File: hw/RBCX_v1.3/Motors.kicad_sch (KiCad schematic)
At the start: 83 parts

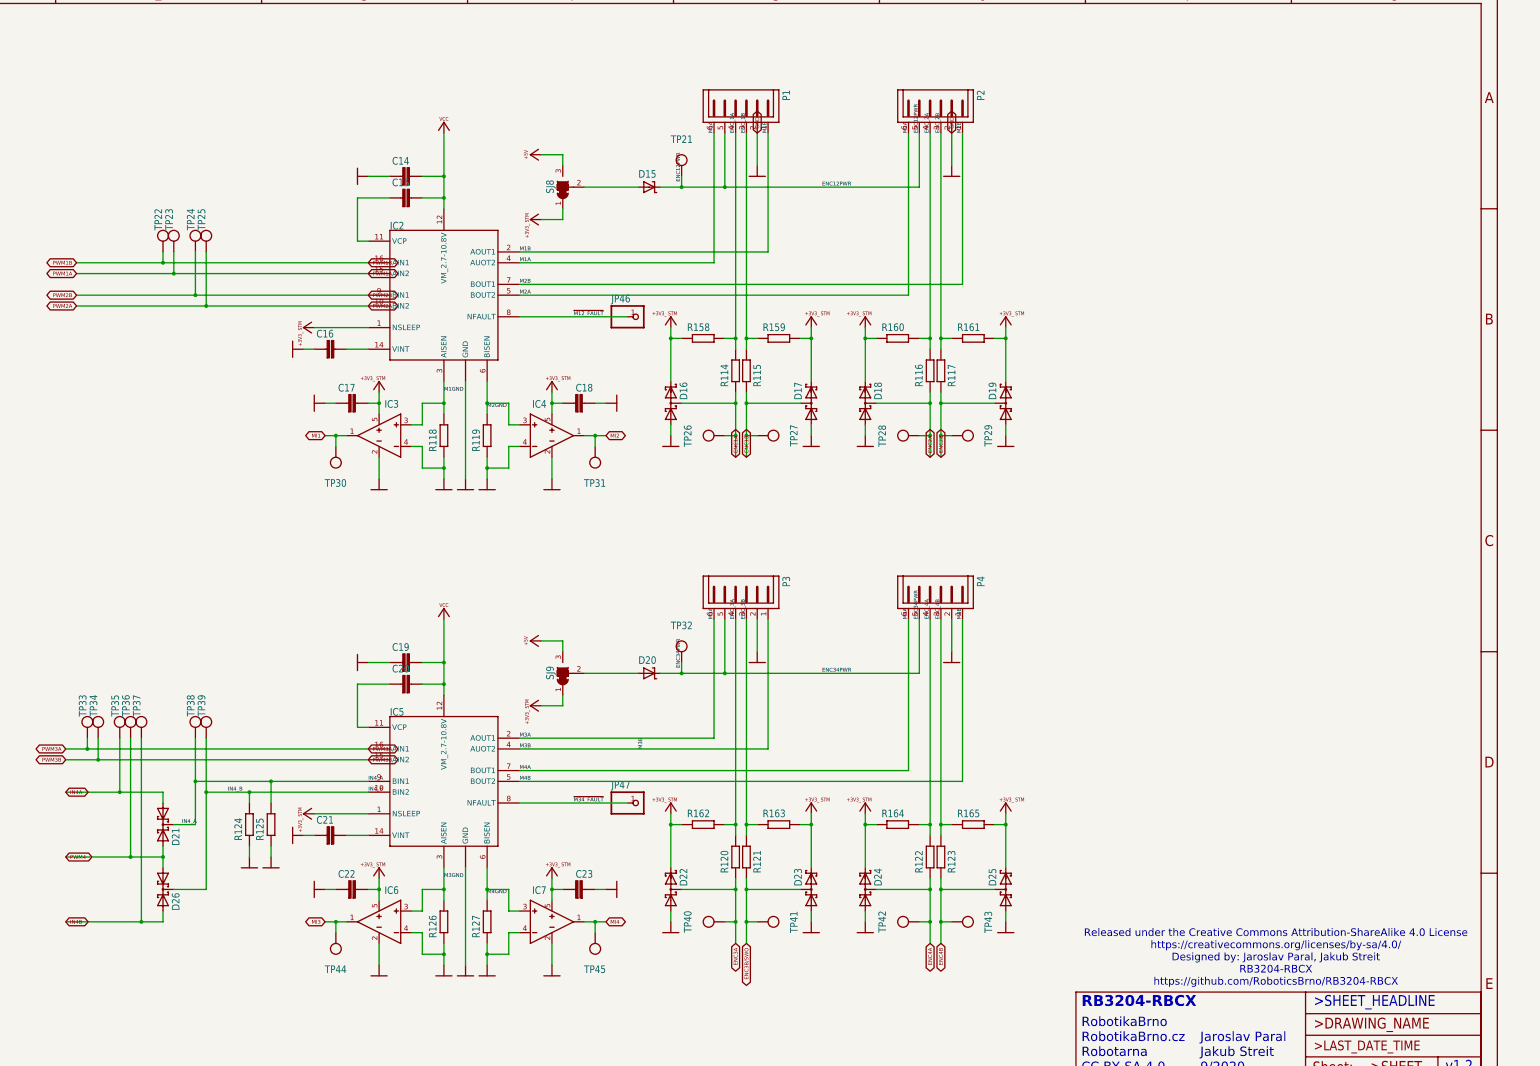
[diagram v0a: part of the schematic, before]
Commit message: Remove stepdowns, Micro-USB; fixup region names
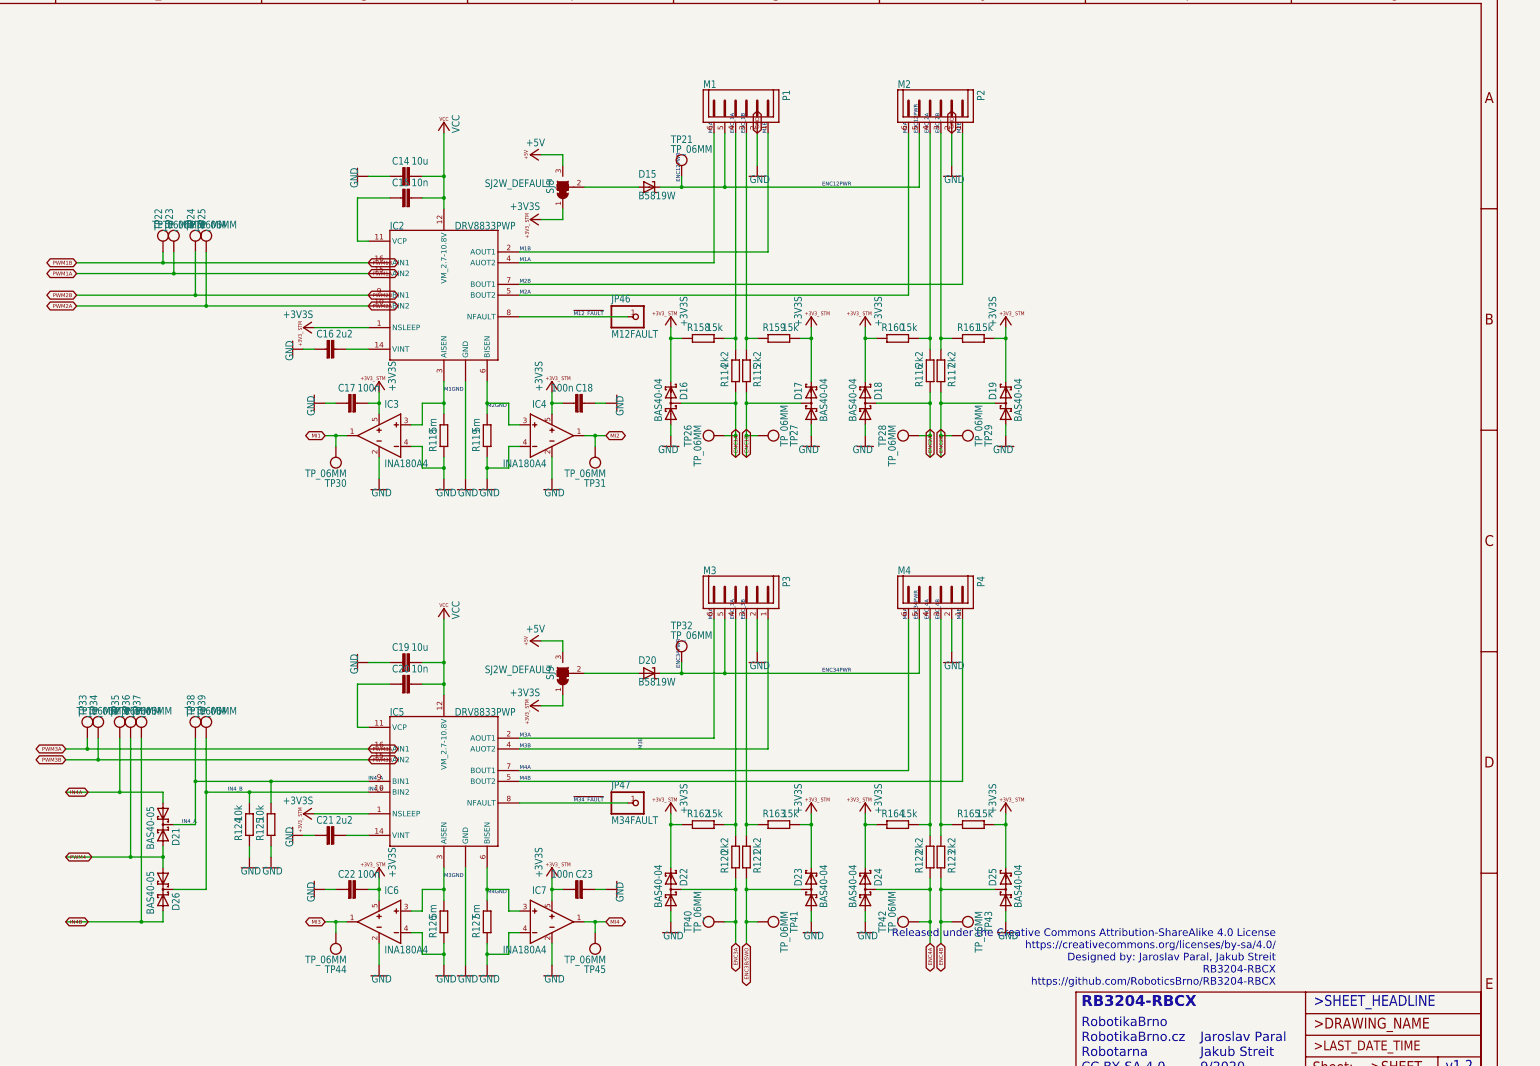
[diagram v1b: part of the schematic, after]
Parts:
- C14, C19: footprint (none) -> RBCX:C0805
- C15, C17, C18, C20, C22, C23: footprint (none) -> RBCX:C0402
- C16, C21: footprint (none) -> RBCX:C0603
- D15, D20: footprint (none) -> RBCX:SOD123
- D16, D17, D18, D19, D22, D23, D24, D25: value (none) -> BAS40-04; footprint (none) -> RBCX:SOT23
- D21, D26: value (none) -> BAS40-05; footprint (none) -> RBCX:SOT23
- IC2, IC5: value (none) -> DRV8833PWP; footprint (none) -> RBCX:HTSSOP
- IC3, IC4, IC6, IC7: footprint (none) -> RBCX:SOT23-5L
- JP46: value (none) -> M12FAULT; footprint (none) -> RBCX:1X01
- JP47: value (none) -> M34FAULT; footprint (none) -> RBCX:1X01
- P1: value (none) -> M1; footprint (none) -> RBCX:JST-PH6
- P2: value (none) -> M2; footprint (none) -> RBCX:JST-PH6
- P3: value (none) -> M3; footprint (none) -> RBCX:JST-PH6
- P4: value (none) -> M4; footprint (none) -> RBCX:JST-PH6
- R114, R115, R116, R117, R120, R121, R122, R123: value (none) -> 2k2; footprint (none) -> RBCX:R0402
- R118, R119, R126, R127: footprint (none) -> RBCX:R1206
- R124, R125: value (none) -> 10k; footprint (none) -> RBCX:R0402
- R158, R159, R160, R161, R162, R163, R164, R165: value (none) -> 15k; footprint (none) -> RBCX:R0402
- SJ8, SJ9: value (none) -> SJ2W_DEFAULT; footprint (none) -> RBCX:SJ_2_DEFAULT
- TP21, TP22, TP23, TP24, TP25, TP26, TP27, TP28, TP29, TP30, TP31, TP32, TP33, TP34, TP35, TP36, TP37, TP38, TP39, TP40, TP41, TP42, TP43, TP44, TP45: value (none) -> TP_06MM; footprint (none) -> RBCX:TP_06
